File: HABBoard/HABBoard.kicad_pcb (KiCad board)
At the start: 4 copper layers, 100 x 100 mm, 211 parts, among them J1 USB_C_MCU, J2 USB_C_GNSS, J3 MEM2067-02-180-00-A_REVB, J4 GPS In, J5 GNSS_UART, J6 DEBUG, J7 VHF Out, J8 UHF Out, Q1 SSM6N7002KFU, Q2 SSM6N7002KFU, Q3 SSM6N7002KFU, Q4 PMN16XNE, SW1 RESET, SW2 BOOT, SW3 USER_BUTTON, SW4 Power, U1 TC2015-3.3VxCTTR, U10 SX1276, U11 SX1276, U12 MP5016GQH-Z, U13 PE42421, U14 ISL91127IR, U15 TPS2116DRLR, U16 INA219BxD, U2 W25Q128JVS, U3 NEO-M9N-00B, U4 AP2138N-2.5, U5 RP2040, U6 BME680, U7 TXS0104E, U8 ICM-20948, U9 AP2138N-1.8, Y1 ECS-TXO-25CSMV-320-BM-TR, Y2 ECS-TXO-25CSMV-320-BM-TR, Y3 12.000MHz

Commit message: PCB Layout Work
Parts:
- Y2: footprint TestPoint:TestPoint_Pad_D1.0mm -> HABParts:OSC_ECS-TXO-25CSMV-320-BM-TR
- moved J8 246.5 mm to (123.0, 97.0)
- moved J7 233.2 mm to (123.0, 50.0)
- moved U8 232.2 mm to (122.8, 75.5)
- moved SW4 226.8 mm to (80.8, 41.5)
- moved U11 224.5 mm to (103.2, 50.0), turned to -90 degrees
- moved U7 218.5 mm to (114.5, 75.5)
- moved C36 216.0 mm to (1.77, -68.5)
- moved D4 211.2 mm to (123.0, 87.0)
- moved R26 207.9 mm to (-5.76, -70.5)
- moved R2 207.5 mm to (-2.85, -70.5)
- moved R24 207.0 mm to (-9.77, -67.5)
- moved C72 206.9 mm to (-1.10, -68.5)
- moved FB1 206.8 mm to (-10.9, -65.0)
- moved J3 206.6 mm to (78.2, 114.8), turned to 180 degrees
- moved C38 203.0 mm to (-13.8, -57.0)
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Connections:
- J4 pad 1: GND -> Net-(J4-Pad1)
- J4 pad G1: Net-(J4-PadG1) -> GND
- J4 pad G2: Net-(J4-PadG1) -> GND
- J4 pad G3: Net-(J4-PadG1) -> GND
- J4 pad G4: Net-(J4-PadG1) -> GND
- L4 pad 2: Net-(J4-PadG1) -> Net-(J4-Pad1)
- U3 pad 11: Net-(J4-PadG1) -> Net-(J4-Pad1)
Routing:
- net /USB_VBUS: track 21.6 -> 0.00 mm, vias 2 -> 0
- net Net-(C53-Pad1): track 18.8 -> 0.00 mm, vias 2 -> 0
- net +SYS: track 18.1 -> 0.00 mm
- net Net-(J1-PadB5): track 10.8 -> 0.00 mm, vias 2 -> 0
- net Net-(BT1-Pad1): track 10.6 -> 0.00 mm
- net Net-(R30-Pad2): track 8.05 -> 0.00 mm
- net Net-(Q4-Pad3): track 7.36 -> 0.00 mm, vias 2 -> 0
- net Net-(Q4-Pad1): track 6.26 -> 0.00 mm
- net Net-(C39-Pad2): track 3.84 -> 0.00 mm
- net Net-(R34-Pad1): track 3.83 -> 0.00 mm
- net Net-(C39-Pad1): track 3.74 -> 0.00 mm
- net Net-(R28-Pad2): track 2.80 -> 0.00 mm
- net Net-(C66-Pad1): track 2.69 -> 0.00 mm
- net +3V3: track 2.42 -> 0.00 mm, vias 1 -> 0
- net Net-(D1-Pad4): track 2.05 -> 0.00 mm
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- added copper zone on In2.Cu, net GND
- removed copper zone on In1.Cu, net GND
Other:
- rule pad_to_mask_clearance: 0.05 -> 0.1

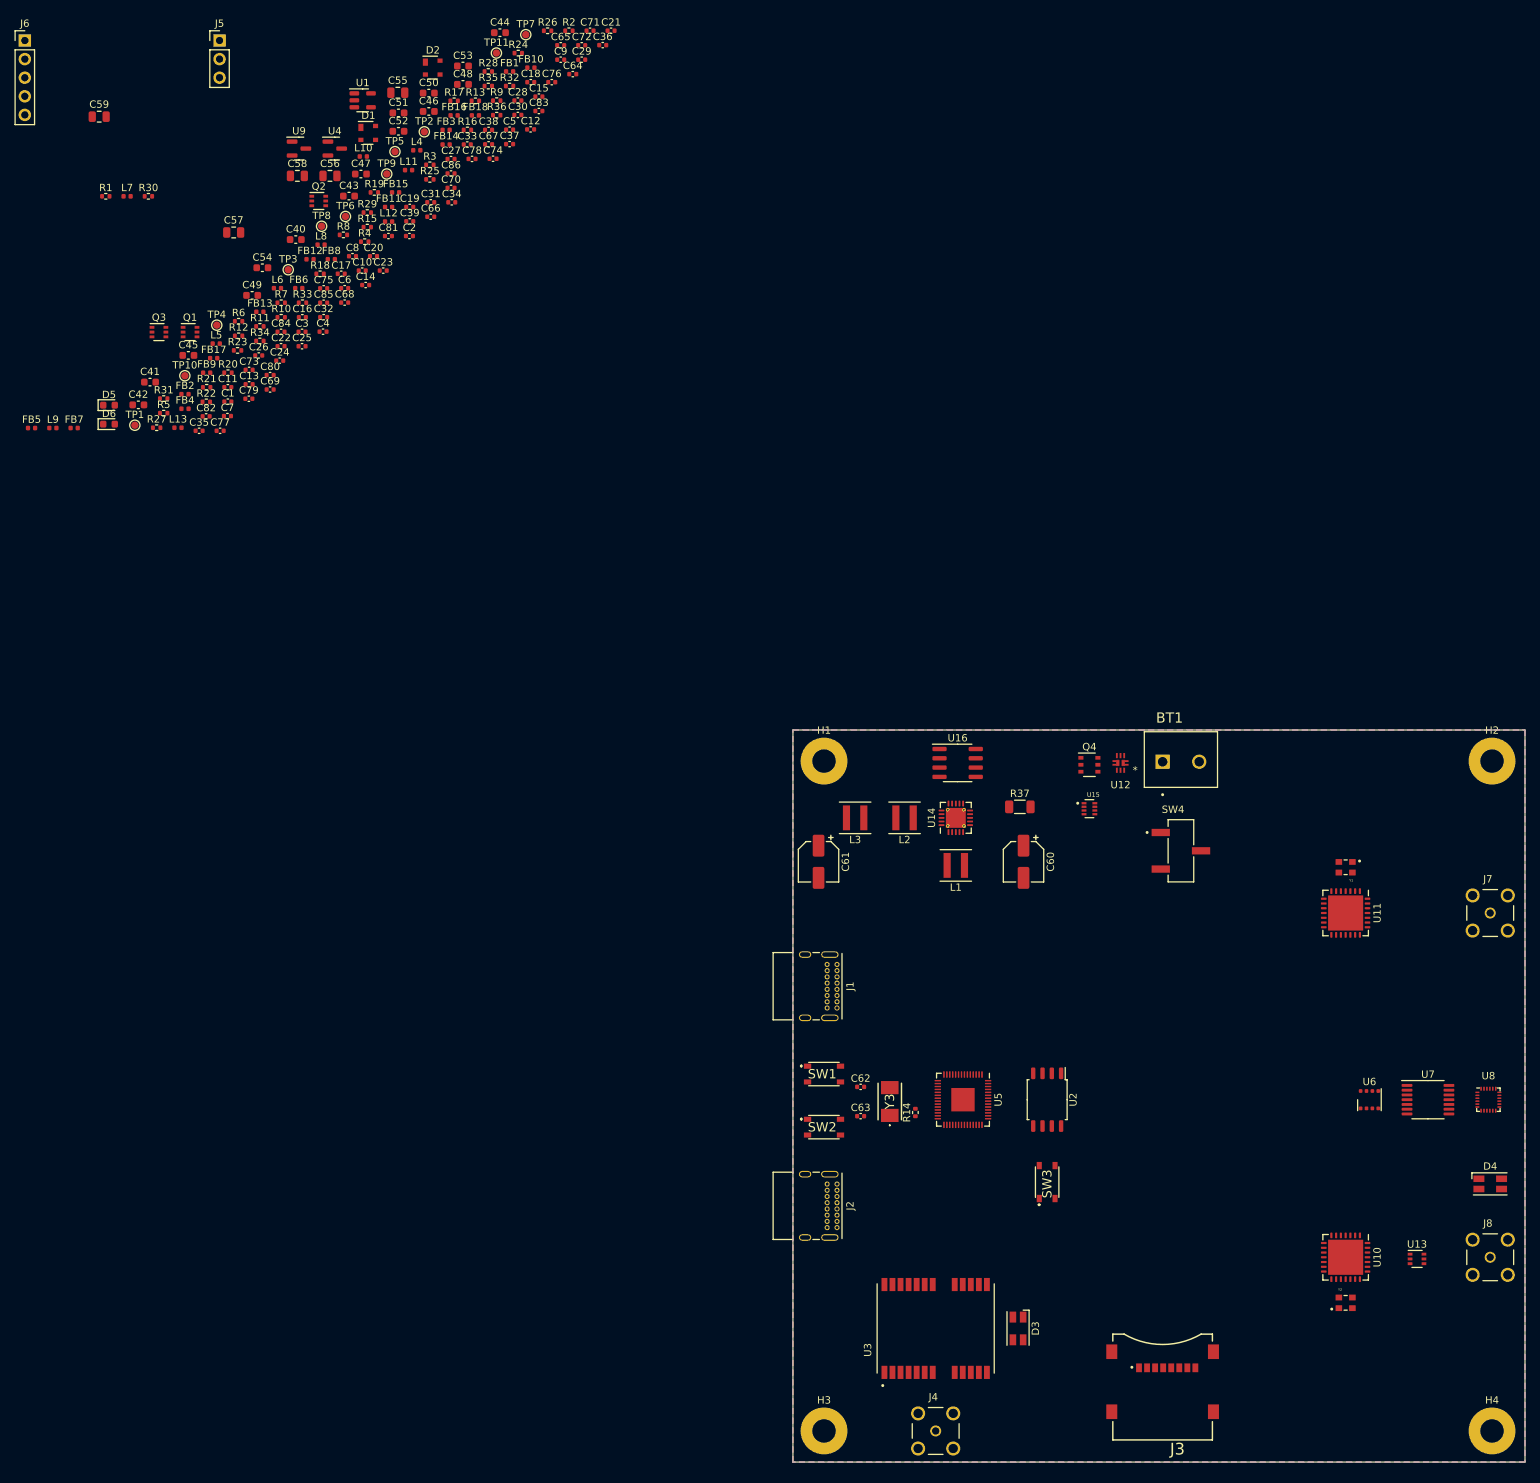
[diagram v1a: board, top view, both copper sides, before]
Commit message: More trace routing
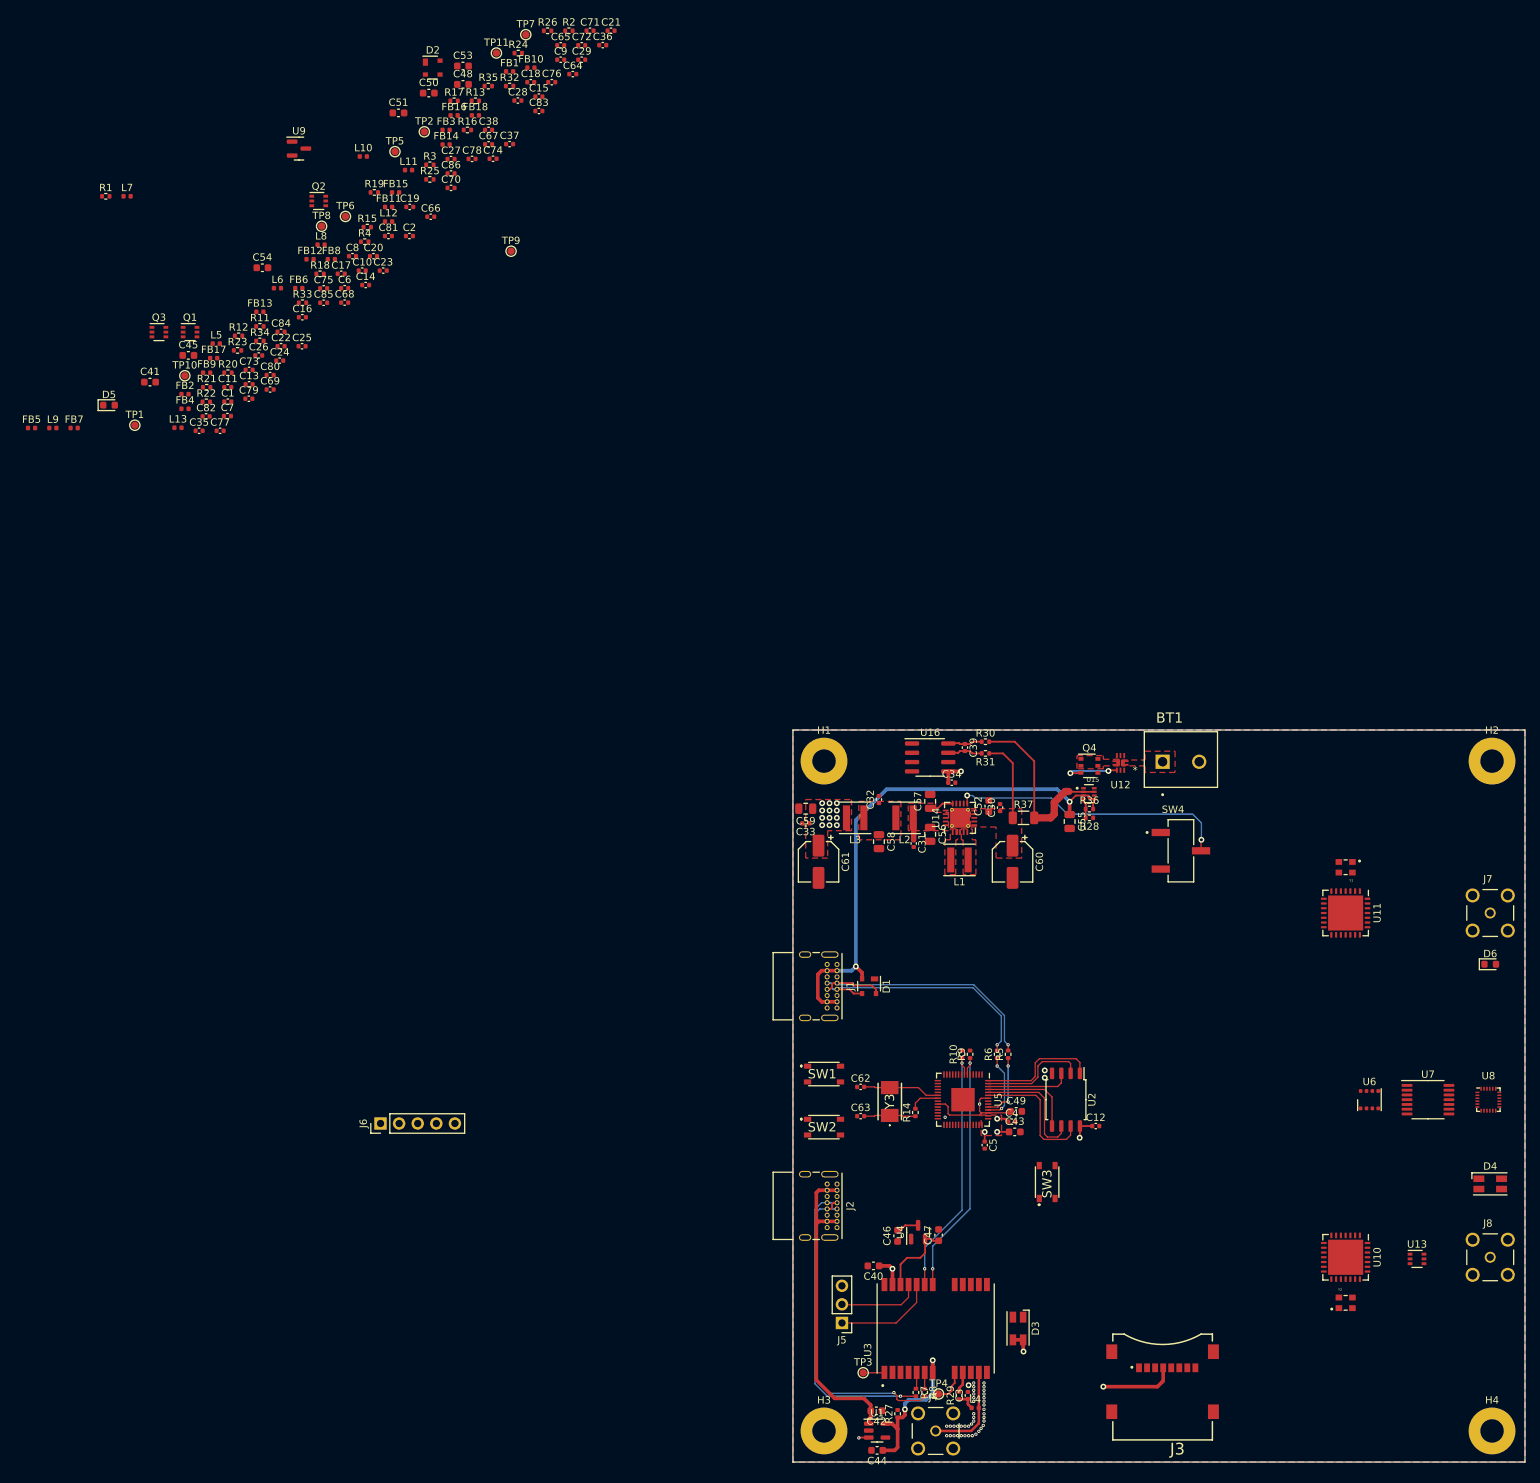
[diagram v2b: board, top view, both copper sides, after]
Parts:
- moved D6 202.6 mm to (123.0, 57.0)
- moved C44 200.4 mm to (39.2, 123.4), turned to 180 degrees
- moved U1 194.8 mm to (39.2, 120.7)
- moved J5 194.7 mm to (34.5, 106.0), turned to 180 degrees
- moved L4 188.0 mm to (52.6, 117.6)
- moved R29 180.7 mm to (50.5, 115.9), turned to 90 degrees
- moved R8 176.9 mm to (45.8, 115.5), turned to -90 degrees
- moved TP4 176.2 mm to (47.6, 115.7)
- moved R7 172.3 mm to (44.5, 115.5), turned to -90 degrees
- moved C3 171.4 mm to (51.6, 115.9), turned to 90 degrees
- moved C42 170.4 mm to (39.1, 118.0), turned to 180 degrees
- moved TP3 169.9 mm to (37.4, 112.8)
- moved R27 168.5 mm to (42.0, 118.4), turned to 90 degrees
- moved U4 168.1 mm to (44.9, 93.6), turned to 90 degrees
- moved C46 166.4 mm to (42.0, 94.1), turned to 90 degrees
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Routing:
- net /USB_VBUS: track 0.00 -> 72.7 mm, vias 0 -> 2
- net Net-(D2-Pad4): track 0.00 -> 43.0 mm, vias 0 -> 1
- net Net-(C42-Pad2): track 0.00 -> 43.0 mm
- net Net-(D2-Pad3): track 0.00 -> 42.4 mm, vias 0 -> 1
- net Net-(SW4-Pad2): track 0.00 -> 38.5 mm, vias 0 -> 2
- net Net-(D1-Pad4): track 0.00 -> 37.9 mm, vias 0 -> 1
- net Net-(D1-Pad3): track 0.00 -> 34.8 mm, vias 0 -> 1
- net /BME_SDA: track 0.00 -> 34.8 mm, vias 0 -> 2
- net /BME_SCL: track 0.00 -> 34.8 mm, vias 0 -> 2
- net +3V3: track 0.00 -> 30.0 mm, vias 0 -> 21
- net Net-(R30-Pad2): track 0.00 -> 25.6 mm
- net Net-(C44-Pad1): track 0.00 -> 21.5 mm, vias 0 -> 2
- net Net-(U2-Pad7): track 0.00 -> 18.1 mm
- net Net-(U2-Pad6): track 0.00 -> 16.6 mm
- net Net-(R13-Pad2): track 0.00 -> 16.6 mm
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- added copper zone on F.Cu, net +3V3
- added copper zone on F.Cu, net +SYS
- added copper zone on F.Cu, net Net-(BT1-Pad1)
- added copper zone on F.Cu, net Net-(C31-Pad1)
- added copper zone on F.Cu, net Net-(C32-Pad1)
- added copper zone on F.Cu, net Net-(L1-Pad1)
- added copper zone on F.Cu, net Net-(L1-Pad2)
- added copper zone on F.Cu, net Net-(Q4-Pad1)

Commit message: More Routing
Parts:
- added J10: RFShield_TwoPieces, HABParts:SMS409F, F.Cu at (100.5, 94.2)
- added J9: RFShield_TwoPieces, HABParts:SMS409F, F.Cu at (100.5, 47.1)
- moved Q2 225.0 mm to (122.1, 111.9), turned to 180 degrees
- moved R19 218.6 mm to (119.2, 111.9), turned to 180 degrees
- moved R20 217.7 mm to (119.2, 113.9), turned to 180 degrees
- moved R21 217.6 mm to (121.5, 109.2), turned to 90 degrees
- moved R22 217.5 mm to (122.7, 109.2), turned to -90 degrees
- moved U9 211.3 mm to (122.8, 80.6), turned to 180 degrees
- moved L9 208.8 mm to (102.0, 97.1)
- moved C51 206.4 mm to (125.8, 80.4), turned to -90 degrees
- moved C50 205.0 mm to (122.6, 83.3), turned to 180 degrees
- moved FB5 201.2 mm to (88.2, 99.7)
- moved C73 200.6 mm to (111.3, 99.6), turned to 90 degrees
- moved L13 199.8 mm to (108.3, 97.1)
- moved C74 198.9 mm to (117.3, 97.1)
- moved L7 198.7 mm to (110.0, 49.4)
- moved C16 197.2 mm to (126.1, 76.1)
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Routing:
- net /BME_SCL: track 34.8 -> 113.9 mm, vias 2 -> 4
- net /BME_SDA: track 34.8 -> 112.3 mm, vias 2 -> 4
- net /SD_SCK: track 0.00 -> 70.5 mm, vias 0 -> 2
- net /SD_MOSI: track 0.00 -> 64.2 mm, vias 0 -> 2
- net /SD_CS: track 0.00 -> 57.4 mm, vias 0 -> 2
- net /MCU_BOOT: track 0.00 -> 49.0 mm, vias 0 -> 2
- net +3V3: track 30.0 -> 74.9 mm, vias 21 -> 39
- net +1V8: track 0.00 -> 42.9 mm, vias 0 -> 4
- net Net-(U10-Pad20): track 0.00 -> 22.5 mm
- net /MCU_RESET: track 0.00 -> 19.8 mm
- net Net-(J6-Pad1): track 0.00 -> 18.6 mm
- net Net-(J6-Pad2): track 0.00 -> 15.2 mm
- net Net-(J1-PadB5): track 0.00 -> 14.4 mm, vias 0 -> 1
- net Net-(J2-PadB5): track 0.00 -> 14.0 mm, vias 0 -> 1
- net Net-(U7-Pad4): track 0.00 -> 14.0 mm
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
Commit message: Even more layout
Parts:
- removed C45: 1u, Capacitor_SMD:C_0603_1608Metric
- removed TP6: VCORE, TestPoint:TestPoint_Pad_D1.0mm
- added C87: 0.1u, Capacitor_SMD:C_0402_1005Metric, F.Cu at (123.8, 71.5)
- moved C15 190.6 mm to (126.1, 75.0)
- moved TP2 183.5 mm to (39.7, 115.9)
- moved Q3 183.2 mm to (77.5, 75.6), turned to 180 degrees
- moved R17 180.3 mm to (57.8, 102.4), turned to -90 degrees
- moved R16 172.9 mm to (60.8, 97.6), turned to 90 degrees
- moved C48 172.5 mm to (43.6, 98.2)
- moved R24 170.6 mm to (77.5, 79.1), turned to 180 degrees
- moved R18 169.6 mm to (59.2, 102.4), turned to 90 degrees
- moved R26 169.0 mm to (80.4, 74.9), turned to 180 degrees
- moved TP5 168.9 mm to (49.7, 96.7)
- moved D5 167.6 mm to (72.5, 75.5), turned to 90 degrees
- moved R15 165.5 mm to (55.9, 97.6), turned to 90 degrees
- moved R23 163.6 mm to (77.5, 77.9), turned to 180 degrees
- moved R25 159.1 mm to (74.6, 76.3), turned to 180 degrees
- moved C21 157.1 mm to (16.7, 86.0)
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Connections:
- J10 pad 10: (no net) -> GND
- J10 pad 11: (no net) -> GND
- J10 pad 12: (no net) -> GND
- J10 pad 13: (no net) -> GND
- J10 pad 14: (no net) -> GND
- J10 pad 15: (no net) -> GND
- J10 pad 16: (no net) -> GND
- J10 pad 2: (no net) -> GND
- J10 pad 3: (no net) -> GND
- J10 pad 4: (no net) -> GND
- J10 pad 5: (no net) -> GND
- J10 pad 6: (no net) -> GND
- J10 pad 7: (no net) -> GND
- J10 pad 8: (no net) -> GND
- J10 pad 9: (no net) -> GND
- J9 pad 10: (no net) -> GND
- J9 pad 11: (no net) -> GND
- J9 pad 12: (no net) -> GND
- J9 pad 13: (no net) -> GND
- J9 pad 14: (no net) -> GND
- J9 pad 15: (no net) -> GND
- J9 pad 16: (no net) -> GND
- J9 pad 2: (no net) -> GND
- J9 pad 3: (no net) -> GND
- J9 pad 4: (no net) -> GND
- J9 pad 5: (no net) -> GND
- J9 pad 6: (no net) -> GND
- J9 pad 7: (no net) -> GND
- J9 pad 8: (no net) -> GND
- J9 pad 9: (no net) -> GND
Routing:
- net /UHF_SRED: track 0.00 -> 92.6 mm, vias 0 -> 4
- net /UHF_SGRN: track 0.00 -> 92.4 mm, vias 0 -> 4
- net /BME_SDA: track 112.3 -> 203.4 mm, vias 4 -> 7
- net +SYS: track 14.3 -> 104.5 mm, vias 0 -> 2
- net /BME_SCL: track 113.9 -> 203.0 mm, vias 4 -> 5
- net /IMU_INT: track 0.00 -> 73.0 mm, vias 0 -> 2
- net /VHF_DIO0: track 0.00 -> 66.4 mm, vias 0 -> 4
- net /VHF_DIO2: track 0.00 -> 65.0 mm, vias 0 -> 6
- net /VHF_DIO1: track 0.00 -> 64.9 mm, vias 0 -> 4
- net /SD_MISO: track 0.00 -> 63.3 mm, vias 0 -> 2
- net /RF_SCK: track 0.00 -> 61.1 mm, vias 0 -> 4
- net /RF_MOSI: track 0.00 -> 57.7 mm, vias 0 -> 4
- net /RF_MISO: track 0.00 -> 57.1 mm, vias 0 -> 4
- net /VHF_RESET: track 0.00 -> 54.9 mm, vias 0 -> 2
- net /VHF_NSS: track 0.00 -> 52.6 mm, vias 0 -> 6
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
